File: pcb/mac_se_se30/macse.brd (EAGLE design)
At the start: 51 x 38 mm, 10 parts, among them J2 ATX24RH

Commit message: added more caps
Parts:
- added C3, C4, C6: 47uF, clock:C1210
- moved C2 0.13 mm to (27.9, 35.5)
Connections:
- net +5V: now also C4.1
- net GND: now also C3.2, C4.2, C6.2
- net N$8: now also C3.1, C6.1
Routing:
- net GND: track 10.9 -> 26.6 mm
- net N$8: track 73.5 -> 64.4 mm
- net +5V: track 46.6 -> 53.7 mm
- net +12V: track 61.5 -> 66.7 mm
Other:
- board text added: "12V"
- board text added: "5V"
- board text added: "PSW"
- board text added: "dekuNukem 2023"
- board text added: "picoRC.com"
- board text removed: "Instructions: picoRC.com"
- board text removed: "PD2 dekuNukem APR 2023"
- board text removed: "PWR SW"

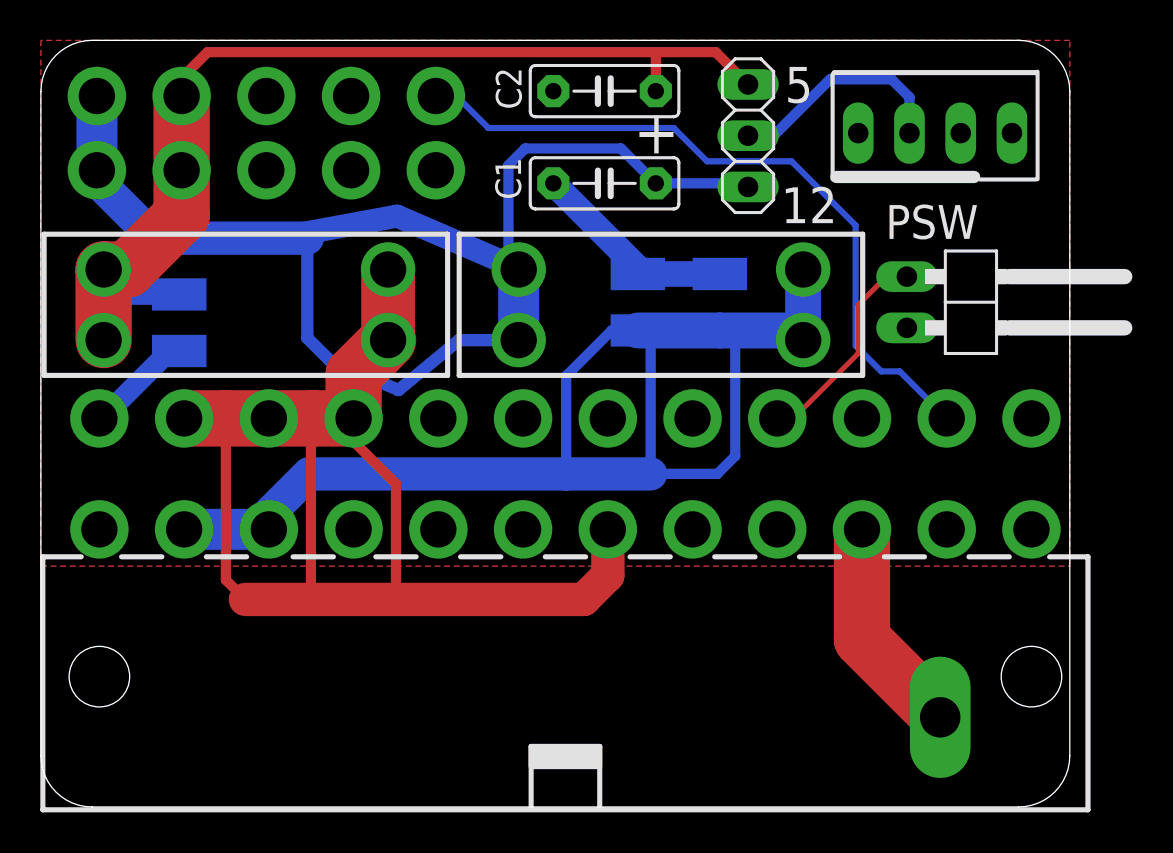
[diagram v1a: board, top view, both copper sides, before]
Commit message: added more caps
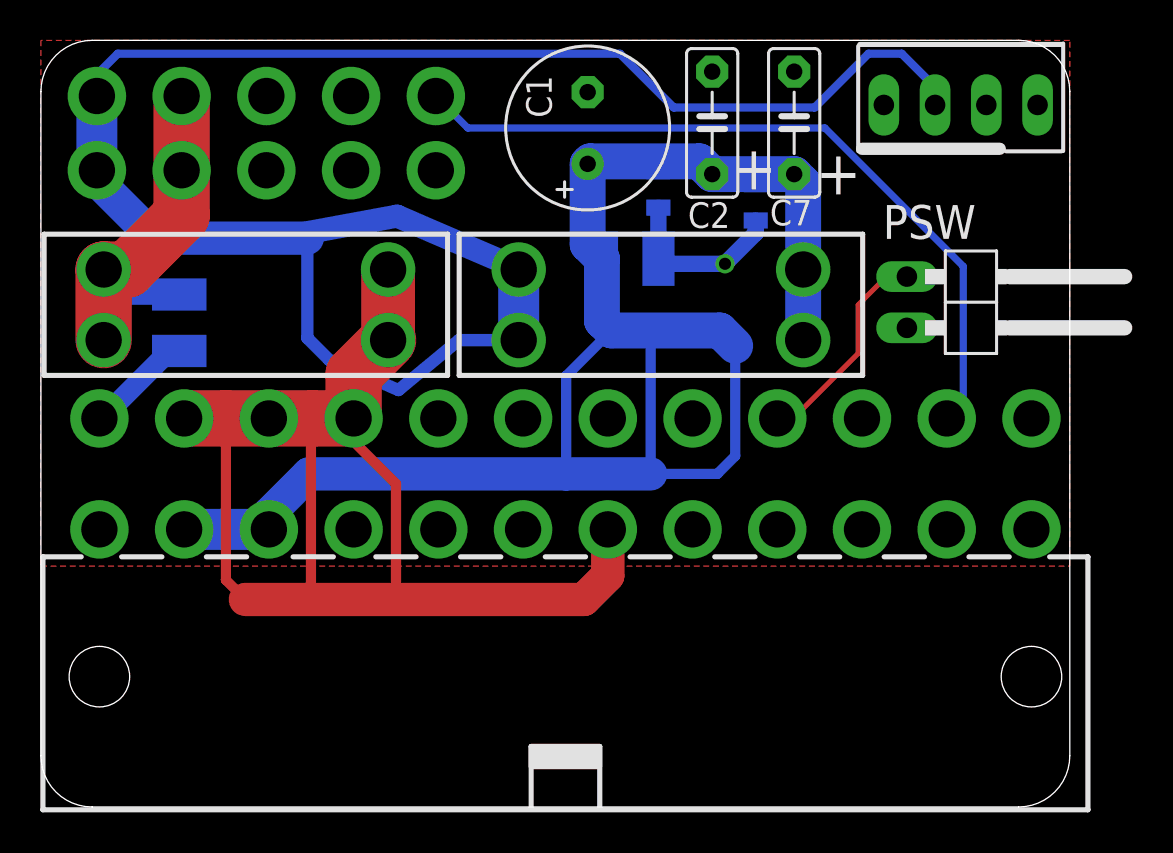
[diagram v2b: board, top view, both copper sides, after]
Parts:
- removed C3: 47uF, clock:C1210
- removed JP4: (no value), pinhead:1X03
- removed TP1: PTR1PAD1-20Y, testpad:P1-20Y
- added C10, C5: 100nF, clock:0805@1
- added C7: (no value), capacitor-wima:C5B2.5
- C1: device capacitor-wima:C5B2.5 -> adafruit_changed:E3,5-8
- moved C2 5.56 mm to (33.3, 33.9), turned to 90 degrees
- moved C1 2.87 mm to (27.1, 33.7), turned to 90 degrees
- moved C6 2.19 mm to (29.2, 27.2), turned to 180 degrees
- moved JP3 1.89 mm to (45.6, 34.8)
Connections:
- removed net N$2: JP3.2, JP4.2
- net +12V: now also JP3.2; no longer C1.1, JP4.1
- net +5V: no longer C2.1, JP4.3
- net GND: now also C1.-, C10.1, C5.1, C7.2; no longer C1.2, C3.2, TP1.TP
- net N$8: now also C1.+, C10.2, C2.1, C5.2, C7.1; no longer C3.1
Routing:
- net +5V: track 53.7 -> 22.5 mm
- net +12V: track 66.7 -> 95.8 mm
- net N$8: track 64.4 -> 88.2 mm
- net GND: track 26.6 -> 14.1 mm, vias 0 -> 1
- net N$2: track 11.3 -> 0.00 mm
- net -12V: track 35.4 -> 37.5 mm
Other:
- board text removed: "12"
- board text removed: "12V"
- board text removed: "5"
- board text removed: "5V"
- board text removed: "GND"
